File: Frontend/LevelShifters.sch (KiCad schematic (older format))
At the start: 61 parts, among them U19 MC33078DGK, U20 MC33078DGK, U21 MC33078DGK, U22 MC33078DGK

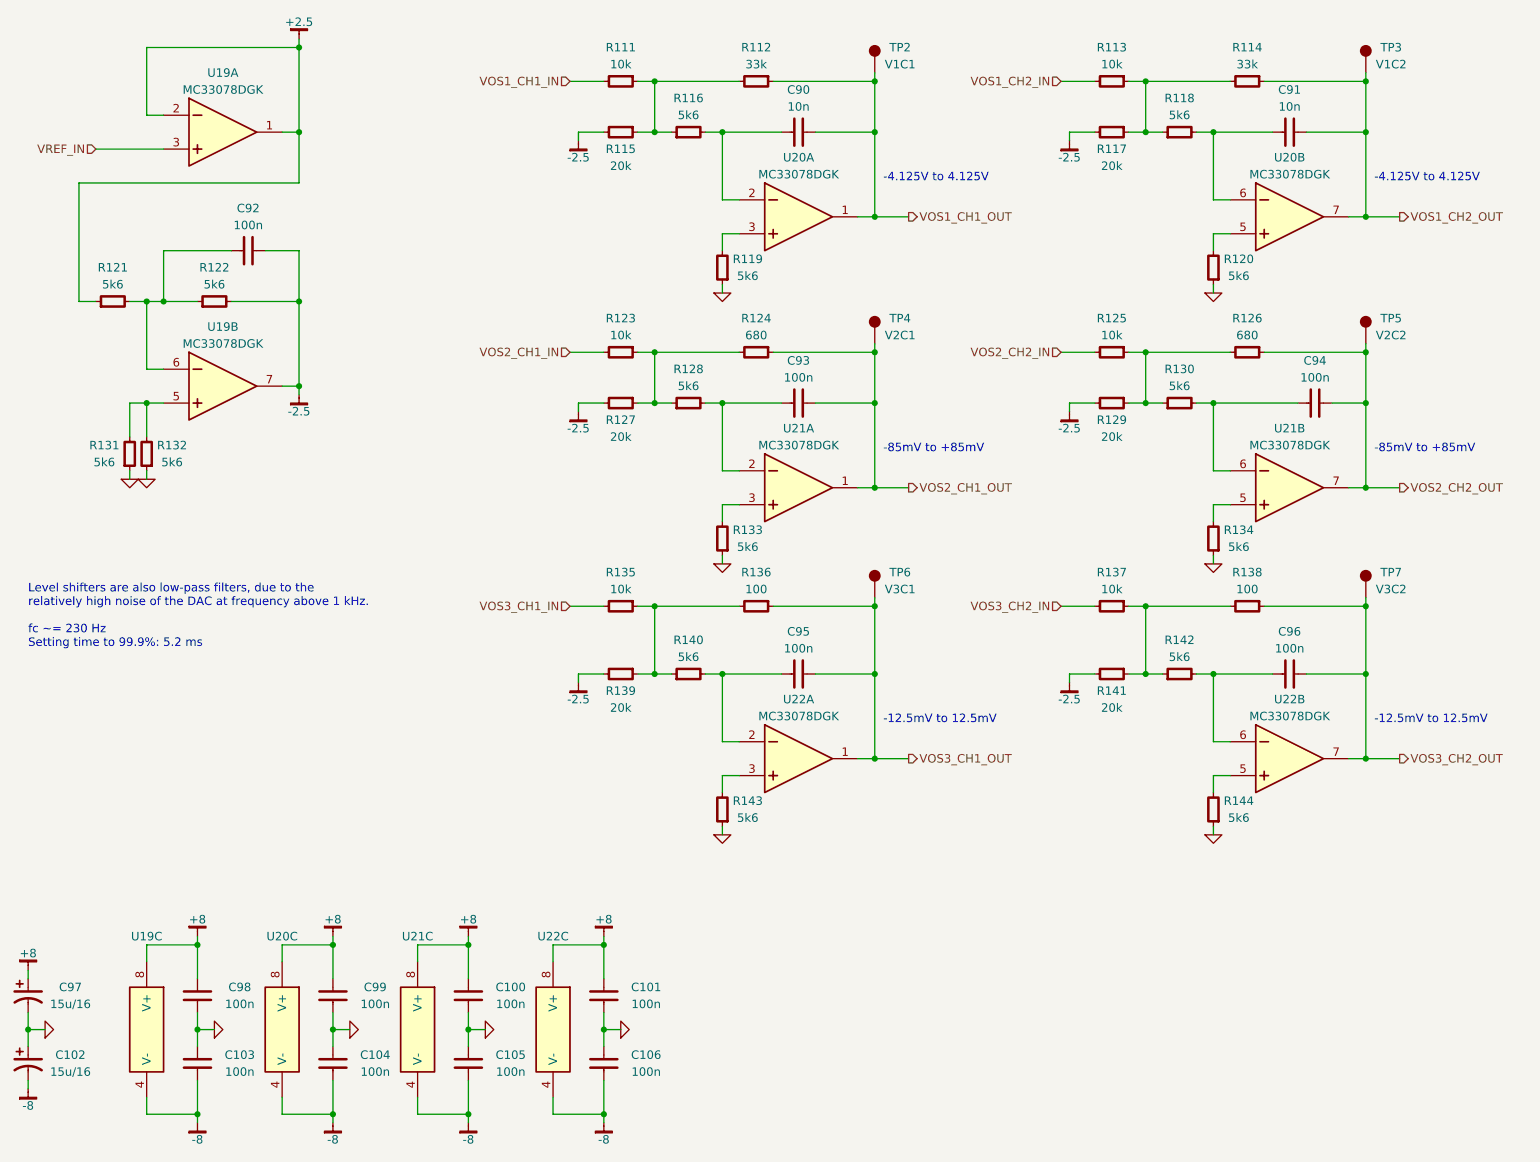
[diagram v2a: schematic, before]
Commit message: Cleanup offset compensation system
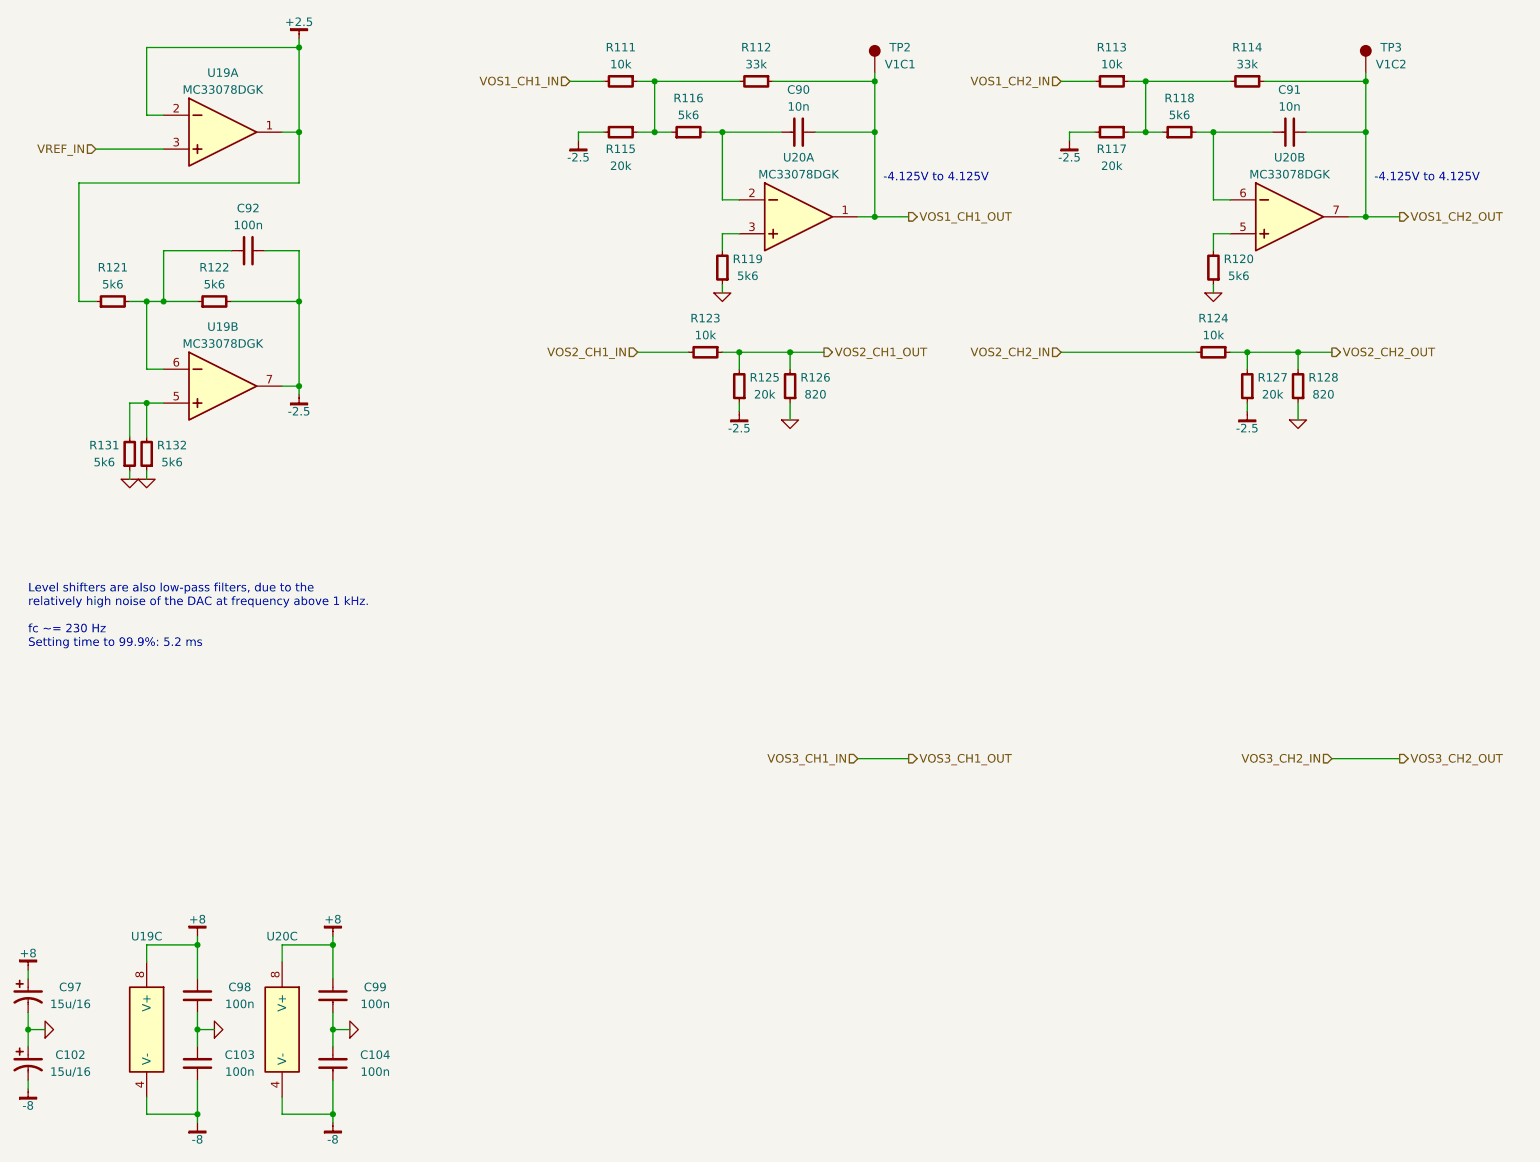
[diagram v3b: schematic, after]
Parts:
- removed C100, C101, C105, C106, C93, C94, C95, C96: 100n, IPC7351-Nominal:CAPC1608X55, symbol C-0603
- removed R129, R139, R141: 20k, IPC7351-Nominal:RESC1005X40, symbol R-0402
- removed R130, R133, R134, R140, R142, R143, R144: 5k6, IPC7351-Nominal:RESC1005X40, symbol R-0402
- removed R135, R137: 10k, IPC7351-Nominal:RESC1005X40, symbol R-0402
- removed R136, R138: 100, IPC7351-Nominal:RESC1005X40, symbol R-0402
- removed TP4: V2C1, conn-test:TEST-SMD-SMALL, symbol TESTPOINT
- removed TP5: V2C2, conn-test:TEST-SMD-SMALL, symbol TESTPOINT
- removed TP6: V3C1, conn-test:TEST-SMD-SMALL, symbol TESTPOINT
- removed TP7: V3C2, conn-test:TEST-SMD-SMALL, symbol TESTPOINT
- removed U21, U22: MC33078DGK, IPC7351-Nominal:SOP65P490X109-8, symbol MC33078DGK
- R124: value 680 -> 10k; BOM RES SMD 680 1% [0402] -> RES SMD 10k 1% [0402]
- R125: value 10k -> 20k; BOM RES SMD 10k 1% [0402] -> RES SMD 20k 1% [0402]
- R126: value 680 -> 820; BOM RES SMD 680 1% [0402] -> RES SMD 820 1% [0402]
- R128: value 5k6 -> 820; BOM RES SMD 5k6 1% [0402] -> RES SMD 820 1% [0402]
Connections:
- net -2.5: now also R125.1, R127.1; no longer R127.2
- net GND: now also R126.1, R128.1
- net VOS2_CH1_OUT: now also R123.1, R125.2, R126.2; no longer R124.1
- net VOS2_CH2_IN: now also R124.2; no longer R125.2
- net VOS2_CH2_OUT: now also R124.1, R127.2, R128.2; no longer R126.1
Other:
- note removed: "-12.5mV to 12.5mV"
- note removed: "-85mV to +85mV"

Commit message: Even more layout tweaks
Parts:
- added C10, C19: 2u2, IPC7351-Nominal:CAPMP2013X120, symbol C-TANT-2012-12
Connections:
- net -2.5: now also C10.2, C19.2
- net VOS2_CH1_OUT: now also C10.1
- net VOS2_CH2_OUT: now also C19.1
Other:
- note removed: "Level shifters are also low-pass filters, due to the\nrelatively high noise of the DAC at frequency above 1 kHz.\n\nfc ~~= 230 Hz\nSetting time to 99.9%: 5.2 ms"
- moved on the sheet: R123, R124, R125, R126, R127, R128

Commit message: More routing adjustments
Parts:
- removed R116, R118: 5k6, IPC7351-Nominal:RESC1005X40, symbol R-0402
- R119, R120, R121, R122, R131, R132: value 5k6 -> 3k3; BOM RES SMD 5k6 1% [0402] -> RES SMD 3k3 1% [0402]
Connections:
- net at C90.2, U20.2 (IN-): now also R111.1, R112.2, R115.1
- net at C91.2, U20.6 (IN-): now also R113.1, R114.2, R117.1
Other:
- moved on the sheet: R111, R113, R115, R117

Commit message: Finally finish the final layout finally
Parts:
- C103, C104, C98, C99: BOM CAP MLCC 100n ≥X5R 16V 20% [0603] -> CAP MLCC 100n ≥X5R 25V 20% [0603]
- C92: BOM CAP MLCC 100n ≥X7R 25V 20% [0603] -> CAP MLCC 100n ≥X5R 25V 20% [0603]
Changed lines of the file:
@@
 P 4900 3650
 AR Path="/552B011F/55501BE9" Ref="#PWR?"  Part="1"
-AR Path="/552B011F/5550176D/55501BE9" Ref="#PWR0319"  Part="1"
-F 0 "#PWR0319" H 4900 3600 30  0001 C CNN
+AR Path="/552B011F/5550176D/55501BE9" Ref="#PWR0317"  Part="1"
+F 0 "#PWR0317" H 4900 3600 30  0001 C CNN
 F 1 "-2.5" H 4900 3550 50  0000 C CNN
 F 2 "" H 4900 3650 60  0000 C CNN
@@
 P 4450 1850
 AR Path="/552B011F/55501C27" Ref="#PWR?"  Part="1"
-AR Path="/552B011F/5550176D/55501C27" Ref="#PWR0320"  Part="1"
-F 0 "#PWR0320" H 4450 1800 30  0001 C CNN
+AR Path="/552B011F/5550176D/55501C27" Ref="#PWR0318"  Part="1"
+F 0 "#PWR0318" H 4450 1800 30  0001 C CNN
 F 1 "-2.5" H 4450 1750 50  0000 C CNN
 F 2 "" H 4450 1850 60  0000 C CNN
@@
 P 5000 2750
 AR Path="/552B011F/55501C2D" Ref="#PWR?"  Part="1"
-AR Path="/552B011F/5550176D/55501C2D" Ref="#PWR0321"  Part="1"
-F 0 "#PWR0321" H 5000 2750 30  0001 C CNN
+AR Path="/552B011F/5550176D/55501C2D" Ref="#PWR0319"  Part="1"
+F 0 "#PWR0319" H 5000 2750 30  0001 C CNN
 F 1 "GND" H 5000 2680 30  0001 C CNN
 F 2 "" H 5000 2750 60  0000 C CNN
@@
 P 7350 1850
 AR Path="/552B011F/55501C3D" Ref="#PWR?"  Part="1"
-AR Path="/552B011F/5550176D/55501C3D" Ref="#PWR0322"  Part="1"
-F 0 "#PWR0322" H 7350 1800 30  0001 C CNN
+AR Path="/552B011F/5550176D/55501C3D" Ref="#PWR0320"  Part="1"
+F 0 "#PWR0320" H 7350 1800 30  0001 C CNN
 F 1 "-2.5" H 7350 1750 50  0000 C CNN
 F 2 "" H 7350 1850 60  0000 C CNN
@@
 P 7900 2750
 AR Path="/552B011F/55501C43" Ref="#PWR?"  Part="1"
-AR Path="/552B011F/5550176D/55501C43" Ref="#PWR0323"  Part="1"
-F 0 "#PWR0323" H 7900 2750 30  0001 C CNN
+AR Path="/552B011F/5550176D/55501C43" Ref="#PWR0321"  Part="1"
+F 0 "#PWR0321" H 7900 2750 30  0001 C CNN
 F 1 "GND" H 7900 2680 30  0001 C CNN
 F 2 "" H 7900 2750 60  0000 C CNN
@@
 F 3 "" H 2190 2475 60  0000 C CNN
 F 4 "Value" H 2200 2500 60  0001 C CNN "Manuf"
-F 5 "CAP MLCC 100n ≥X7R 25V 20% [0603]" H 3000 3050 60  0001 C CNN "BOM"
+F 5 "CAP MLCC 100n ≥X5R 25V 20% [0603]" H 3000 3050 60  0001 C CNN "BOM"
 	1    2200 2500
 	0    1    1    0
@@
 P 2500 1250
 AR Path="/552B011F/55501C81" Ref="#PWR?"  Part="1"
-AR Path="/552B011F/5550176D/55501C81" Ref="#PWR0324"  Part="1"
-F 0 "#PWR0324" H 2500 1300 30  0001 C CNN
+AR Path="/552B011F/5550176D/55501C81" Ref="#PWR0322"  Part="1"
+F 0 "#PWR0322" H 2500 1300 30  0001 C CNN
 F 1 "+2.5" H 2500 1350 50  0000 C CNN
 F 2 "" H 2500 1250 60  0000 C CNN
@@
 P 1600 3850
 AR Path="/552B011F/55501D6D" Ref="#PWR?"  Part="1"
-AR Path="/552B011F/5550176D/55501D6D" Ref="#PWR0325"  Part="1"
-F 0 "#PWR0325" H 1600 3850 30  0001 C CNN
+AR Path="/552B011F/5550176D/55501D6D" Ref="#PWR0323"  Part="1"
+F 0 "#PWR0323" H 1600 3850 30  0001 C CNN
 F 1 "GND" H 1600 3780 30  0001 C CNN
 F 2 "" H 1600 3850 60  0000 C CNN
@@
 P 1500 3850
 AR Path="/552B011F/55501D74" Ref="#PWR?"  Part="1"
-AR Path="/552B011F/5550176D/55501D74" Ref="#PWR0326"  Part="1"
-F 0 "#PWR0326" H 1500 3850 30  0001 C CNN
+AR Path="/552B011F/5550176D/55501D74" Ref="#PWR0324"  Part="1"
+F 0 "#PWR0324" H 1500 3850 30  0001 C CNN
 F 1 "GND" H 1500 3780 30  0001 C CNN
 F 2 "" H 1500 3850 60  0000 C CNN
@@
 P 2000 7100
 AR Path="/552B011F/55504415" Ref="#PWR?"  Part="1"
-AR Path="/552B011F/5550176D/55504415" Ref="#PWR0327"  Part="1"
-F 0 "#PWR0327" H 2000 7100 30  0001 C CNN
+AR Path="/552B011F/5550176D/55504415" Ref="#PWR0325"  Part="1"
+F 0 "#PWR0325" H 2000 7100 30  0001 C CNN
 F 1 "GND" H 2000 7030 30  0001 C CNN
 F 2 "" H 2000 7100 60  0000 C CNN
@@
 P 2800 7100
 AR Path="/552B011F/5550441B" Ref="#PWR?"  Part="1"
-AR Path="/552B011F/5550176D/5550441B" Ref="#PWR0328"  Part="1"
-F 0 "#PWR0328" H 2800 7100 30  0001 C CNN
+AR Path="/552B011F/5550176D/5550441B" Ref="#PWR0326"  Part="1"
+F 0 "#PWR0326" H 2800 7100 30  0001 C CNN
 F 1 "GND" H 2800 7030 30  0001 C CNN
 F 2 "" H 2800 7100 60  0000 C CNN
@@
 P 1900 6550
 AR Path="/552B011F/55504479" Ref="#PWR?"  Part="1"
-AR Path="/552B011F/5550176D/55504479" Ref="#PWR0329"  Part="1"
-F 0 "#PWR0329" H 1900 6600 30  0001 C CNN
+AR Path="/552B011F/5550176D/55504479" Ref="#PWR0327"  Part="1"
+F 0 "#PWR0327" H 1900 6600 30  0001 C CNN
 F 1 "+8" H 1900 6650 50  0000 C CNN
 F 2 "" H 1900 6550 60  0000 C CNN
@@
 P 2700 6550
 AR Path="/552B011F/5550447F" Ref="#PWR?"  Part="1"
-AR Path="/552B011F/5550176D/5550447F" Ref="#PWR0330"  Part="1"
-F 0 "#PWR0330" H 2700 6600 30  0001 C CNN
+AR Path="/552B011F/5550176D/5550447F" Ref="#PWR0328"  Part="1"
+F 0 "#PWR0328" H 2700 6600 30  0001 C CNN
 F 1 "+8" H 2700 6650 50  0000 C CNN
 F 2 "" H 2700 6550 60  0000 C CNN
@@
 P 2700 7650
 AR Path="/552B011F/5550449D" Ref="#PWR?"  Part="1"
-AR Path="/552B011F/5550176D/5550449D" Ref="#PWR0331"  Part="1"
-F 0 "#PWR0331" H 2700 7600 30  0001 C CNN
+AR Path="/552B011F/5550176D/5550449D" Ref="#PWR0329"  Part="1"
+F 0 "#PWR0329" H 2700 7600 30  0001 C CNN
 F 1 "-8" H 2700 7550 50  0000 C CNN
 F 2 "" H 2700 7650 60  0000 C CNN
@@
 P 1900 7650
 AR Path="/552B011F/555044A3" Ref="#PWR?"  Part="1"
-AR Path="/552B011F/5550176D/555044A3" Ref="#PWR0332"  Part="1"
-F 0 "#PWR0332" H 1900 7600 30  0001 C CNN
+AR Path="/552B011F/5550176D/555044A3" Ref="#PWR0330"  Part="1"
+F 0 "#PWR0330" H 1900 7600 30  0001 C CNN
 F 1 "-8" H 1900 7550 50  0000 C CNN
 F 2 "" H 1900 7650 60  0000 C CNN
@@
 F 3 "" H 1890 6875 60  0000 C CNN
 F 4 "Value" H 1900 6900 60  0001 C CNN "Manuf"
-F 5 "CAP MLCC 100n ≥X5R 16V 20% [0603]" H 2700 7450 60  0001 C CNN "BOM"
+F 5 "CAP MLCC 100n ≥X5R 25V 20% [0603]" H 2700 7450 60  0001 C CNN "BOM"
 	1    1900 6900
 	1    0    0    -1
@@
 F 3 "" H 1890 7275 60  0000 C CNN
 F 4 "Value" H 1900 7300 60  0001 C CNN "Manuf"
-F 5 "CAP MLCC 100n ≥X5R 16V 20% [0603]" H 2700 7850 60  0001 C CNN "BOM"
+F 5 "CAP MLCC 100n ≥X5R 25V 20% [0603]" H 2700 7850 60  0001 C CNN "BOM"
 	1    1900 7300
 	1    0    0    -1
@@
 F 3 "" H 2690 7275 60  0000 C CNN
 F 4 "Value" H 2700 7300 60  0001 C CNN "Manuf"
-F 5 "CAP MLCC 100n ≥X5R 16V 20% [0603]" H 3500 7850 60  0001 C CNN "BOM"
+F 5 "CAP MLCC 100n ≥X5R 25V 20% [0603]" H 3500 7850 60  0001 C CNN "BOM"
 	1    2700 7300
 	1    0    0    -1
@@
 F 3 "" H 2690 6875 60  0000 C CNN
 F 4 "Value" H 2700 6900 60  0001 C CNN "Manuf"
-F 5 "CAP MLCC 100n ≥X5R 16V 20% [0603]" H 3500 7450 60  0001 C CNN "BOM"
+F 5 "CAP MLCC 100n ≥X5R 25V 20% [0603]" H 3500 7450 60  0001 C CNN "BOM"
 	1    2700 6900
 	1    0    0    -1
@@
 	1200 2800 1300 2800
 $Comp
-L -2.5 #PWR0333
+L -2.5 #PWR0331
 U 1 1 55509AF5
 P 2500 3350
-F 0 "#PWR0333" H 2500 3300 30  0001 C CNN
+F 0 "#PWR0331" H 2500 3300 30  0001 C CNN
 F 1 "-2.5" H 2500 3250 50  0000 C CNN
 F 2 "" H 2500 3350 60  0000 C CNN
@@
 P 1000 7100
 AR Path="/552B011F/55557C19" Ref="#PWR?"  Part="1"
-AR Path="/552B011F/5550176D/55557C19" Ref="#PWR0334"  Part="1"
-F 0 "#PWR0334" H 1000 7100 30  0001 C CNN
+AR Path="/552B011F/5550176D/55557C19" Ref="#PWR0332"  Part="1"
+F 0 "#PWR0332" H 1000 7100 30  0001 C CNN
 F 1 "GND" H 1000 7030 30  0001 C CNN
 F 2 "" H 1000 7100 60  0000 C CNN
@@
 P 900 6750
 AR Path="/552B011F/55557E5D" Ref="#PWR?"  Part="1"
-AR Path="/552B011F/5550176D/55557E5D" Ref="#PWR0335"  Part="1"
-F 0 "#PWR0335" H 900 6800 30  0001 C CNN
+AR Path="/552B011F/5550176D/55557E5D" Ref="#PWR0333"  Part="1"
+F 0 "#PWR0333" H 900 6800 30  0001 C CNN
 F 1 "+8" H 900 6850 50  0000 C CNN
 F 2 "" H 900 6750 60  0000 C CNN
@@
 P 900 7450
 AR Path="/552B011F/55558024" Ref="#PWR?"  Part="1"
-AR Path="/552B011F/5550176D/55558024" Ref="#PWR0336"  Part="1"
-F 0 "#PWR0336" H 900 7400 30  0001 C CNN
+AR Path="/552B011F/5550176D/55558024" Ref="#PWR0334"  Part="1"
+F 0 "#PWR0334" H 900 7400 30  0001 C CNN
 F 1 "-8" H 900 7350 50  0000 C CNN
 F 2 "" H 900 7450 60  0000 C CNN
@@
 Connection ~ 4900 3300
 $Comp
-L GND #PWR0337
+L GND #PWR0335
 U 1 1 555B7B2D
 P 5200 3700
-F 0 "#PWR0337" H 5200 3700 30  0001 C CNN
+F 0 "#PWR0335" H 5200 3700 30  0001 C CNN
 F 1 "GND" H 5200 3630 30  0001 C CNN
 F 2 "" H 5200 3700 60  0000 C CNN
@@
 P 7750 3650
 AR Path="/552B011F/555BC6E4" Ref="#PWR?"  Part="1"
-AR Path="/552B011F/5550176D/555BC6E4" Ref="#PWR0338"  Part="1"
-F 0 "#PWR0338" H 7750 3600 30  0001 C CNN
+AR Path="/552B011F/5550176D/555BC6E4" Ref="#PWR0336"  Part="1"
+F 0 "#PWR0336" H 7750 3600 30  0001 C CNN
 F 1 "-2.5" H 7750 3550 50  0000 C CNN
 F 2 "" H 7750 3650 60  0000 C CNN
@@
 Connection ~ 7750 3300
 $Comp
-L GND #PWR0339
+L GND #PWR0337
 U 1 1 555BC706
 P 8050 3700
-F 0 "#PWR0339" H 8050 3700 30  0001 C CNN
+F 0 "#PWR0337" H 8050 3700 30  0001 C CNN
 F 1 "GND" H 8050 3630 30  0001 C CNN
 F 2 "" H 8050 3700 60  0000 C CNN
@@
 P 5550 3650
 AR Path="/552B011F/5566954E" Ref="#PWR?"  Part="1"
-AR Path="/552B011F/5550176D/5566954E" Ref="#PWR0340"  Part="1"
-F 0 "#PWR0340" H 5550 3600 30  0001 C CNN
+AR Path="/552B011F/5550176D/5566954E" Ref="#PWR0338"  Part="1"
+F 0 "#PWR0338" H 5550 3600 30  0001 C CNN
 F 1 "-2.5" H 5550 3550 50  0000 C CNN
 F 2 "" H 5550 3650 60  0000 C CNN
@@
 P 8400 3650
 AR Path="/552B011F/5566970D" Ref="#PWR?"  Part="1"
-AR Path="/552B011F/5550176D/5566970D" Ref="#PWR0341"  Part="1"
-F 0 "#PWR0341" H 8400 3600 30  0001 C CNN
+AR Path="/552B011F/5550176D/5566970D" Ref="#PWR0339"  Part="1"
+F 0 "#PWR0339" H 8400 3600 30  0001 C CNN
 F 1 "-2.5" H 8400 3550 50  0000 C CNN
 F 2 "" H 8400 3650 60  0000 C CNN
